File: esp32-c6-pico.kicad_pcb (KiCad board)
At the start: 4 copper layers, 20 x 29 mm, 65 parts, among them J1 USB4105-GF-A, J2 J2 GPIO / 2.00mm, J3 J3 GPIO / 2.00mm, SW1 RESET, SW2 BOOT, U1 ESP32-C6, U2 AP2112K-3.3, U3 W25Q32JVZPIQ, U4 SN74LV1T125, Y1 40MHz / CL=8pF

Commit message: optimize crystal rounting
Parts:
- moved R18 1.21 mm to (114.2, 115.0)
- moved C15 0.65 mm to (112.7, 114.7), turned to 90 degrees
- moved C4 0.59 mm to (116.1, 115.0), turned to 0 degrees
- moved C14 0.53 mm to (113.2, 117.4), turned to 90 degrees
- moved Y1 0.37 mm to (115.3, 116.9)
- moved C5 0.35 mm to (115.4, 118.8)
- moved C17 0.25 mm to (114.7, 113.0)
- moved C2 0.10 mm to (112.5, 113.0)
- moved L3 0.06 mm to (113.6, 113.4)
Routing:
- net USB_D-: track 33.3 -> 24.7 mm
- net GND: track 32.7 -> 27.5 mm, vias 48 -> 38
- net XTAL_LOAD_P: track 4.92 -> 2.38 mm
- net USB_D+: track 22.4 -> 24.1 mm
- net +3V3: track 69.4 -> 67.9 mm
- net XTAL_P: track 1.18 -> 2.47 mm
- net RF_50: track 3.48 -> 2.61 mm
- net VBUS_USB: track 40.7 -> 39.9 mm
- net XTAL_N: track 5.75 -> 5.21 mm

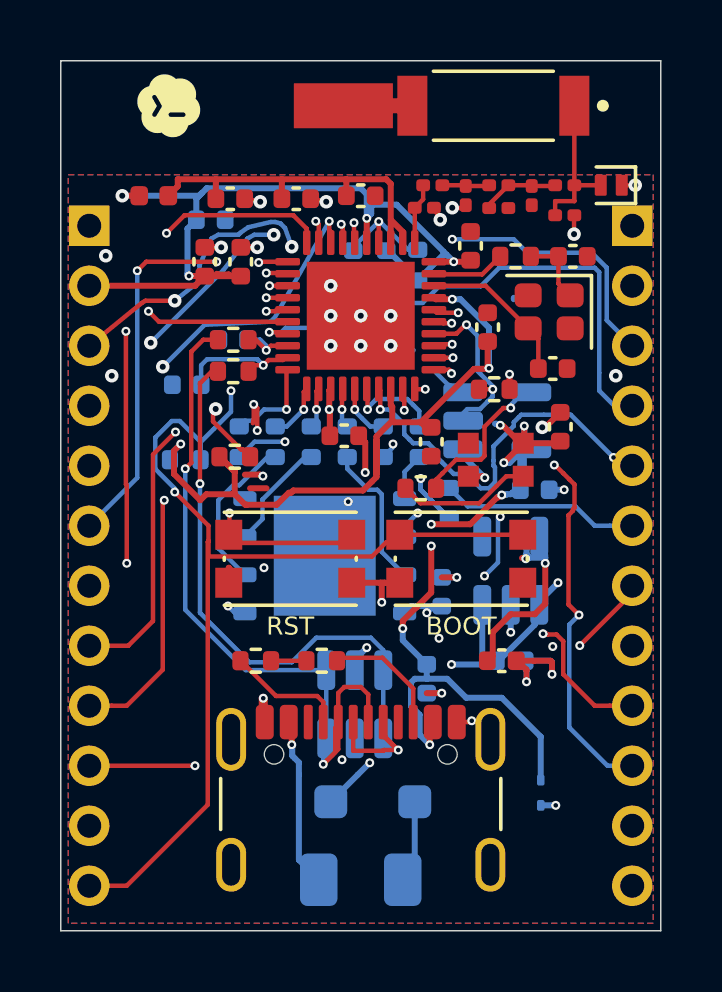
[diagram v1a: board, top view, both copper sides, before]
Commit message: Move headers inward by 0.3 mm and refresh layout outputs
Keep the 20 x 29 mm outline and move J2/J3 inward to a 17.50 mm
column spacing. Adjust local routing and labels, then refresh placement,
previews, geometry checks and fabrication notes. Preserve the subsequent
back-logo move and corrected drawing dimensions.

Validation: DRC, unconnected items and schematic parity all zero.
Independent QA passes 44/49 checks; the five failures predate this change.
Verified the input baseline and kept schematic, rules and RF/XTAL/USB
routing unchanged.
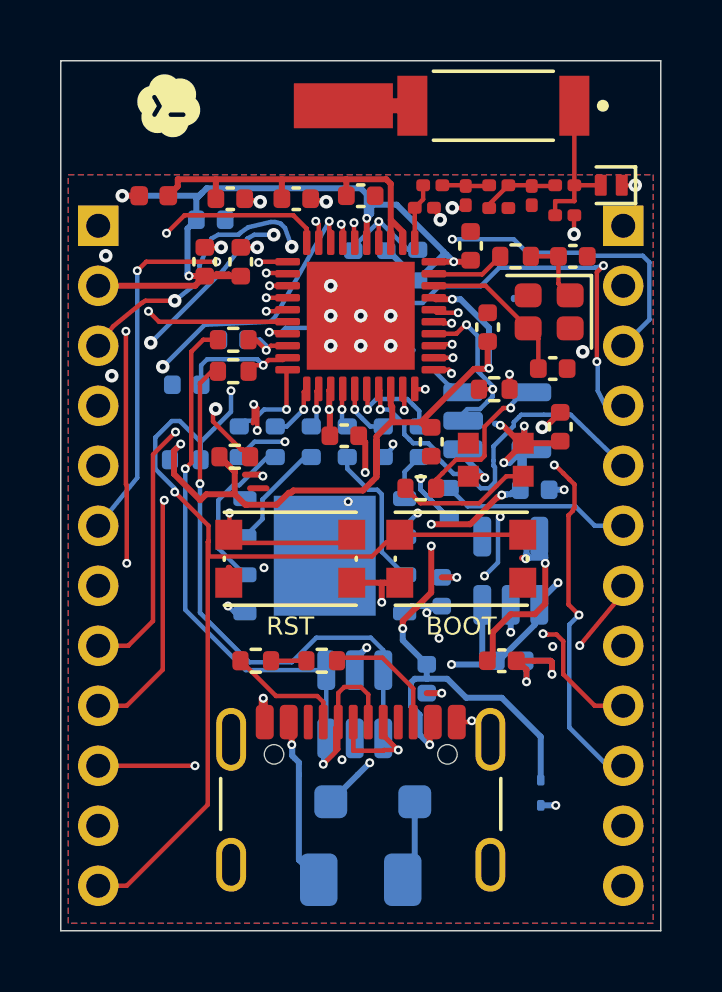
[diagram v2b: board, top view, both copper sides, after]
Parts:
- moved J2 0.30 mm to (100.2, 114.0)
- moved J3 0.30 mm to (117.8, 114.0)
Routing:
- net GPIO10: track 25.6 -> 27.2 mm
- net +5V: track 26.1 -> 27.6 mm
- net GPIO15: track 13.1 -> 12.7 mm, vias 2 -> 1
- net GPIO11: track 18.0 -> 18.3 mm, vias 1 -> 3
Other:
- board text added: "20 x 29 mm | 4 layers | 0.8 mm nominal | 0.20 mm drilled vias"
- board text removed: "20.5 x 32 mm | 4 layers | 0.8 mm nominal | 0.20 mm drilled vias"

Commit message: optimize USB vbus routing and other
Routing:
- net GND: track 27.5 -> 22.6 mm, vias 38 -> 36
- net VBUS_USB: track 39.9 -> 37.2 mm, vias 10 -> 8
- net GPIO20: track 19.6 -> 18.6 mm
- net GPIO15: track 12.7 -> 12.0 mm
- net U0TXD_MCU: track 7.38 -> 6.66 mm

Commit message: Restore SOIC-8 flash, shrink USB diode and remove input fuse
Use W25Q32JVSNIQ in a 150 mil SOIC-8 footprint and BAT760-7 in
SOD-323. Remove F1 and connect USB VBUS directly to the blocking
diode. Preserve the board outline and RF, crystal and USB data routing.

Synchronize schematics, BOM, placement, previews, fabrication notes and
independent checks. ERC, DRC, unconnected items and schematic parity
are all zero. QA passes 45 of 51 checks, retaining six pre-existing failures.
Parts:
- removed F1: 0.75A hold, Fuse:Fuse_1206_3216Metric
- D5: value SS14FL -> BAT760-7; footprint Diode_SMD:D_SOD-123F -> Diode_SMD:D_SOD-323
- U3: value W25Q32JVZPIQ -> W25Q32JVSNIQ; footprint Package_SON:WSON-8-1EP_6x5mm_P1.27mm_EP3.4x4mm -> Package_SO:SOIC-8_3.9x4.9mm_P1.27mm
- moved U3 0.22 mm to (107.6, 124.9)
- moved C6 0.10 mm to (111.8, 126.2)
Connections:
- D5 pad 2: VBUS_FUSED -> VBUS_USB
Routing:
- net VBUS_FUSED: track 2.77 -> 0.00 mm
- net SPI_CLK: track 4.18 -> 6.18 mm, vias 2 -> 0
- net U0TXD_MCU: track 6.66 -> 4.93 mm
- net VBUS_USB: track 37.2 -> 38.7 mm
- net SPI_CS: track 8.66 -> 7.22 mm
- net SPI_HD: track 4.89 -> 5.74 mm, vias 0 -> 2
- net SPI_Q: track 5.35 -> 6.04 mm

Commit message: move L2 into B.Cu and optimize routing
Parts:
- L2: moved to B.Cu
- moved L2 9.46 mm to (111.5, 112.7), turned to 180 degrees
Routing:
- net GPIO9_BOOT: track 38.3 -> 34.9 mm
- net +3V3: track 67.7 -> 66.5 mm, vias 9 -> 8
- net V3A: track 12.6 -> 11.8 mm, vias 0 -> 1
- net GPIO10: track 27.2 -> 26.6 mm
- net GPIO2: track 12.7 -> 13.3 mm
- net GND: vias 36 -> 35

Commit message: Complete first PCB revision
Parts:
- removed C26: 100nF, Capacitor_SMD:C_0402_1005Metric
- removed C27, C28: DNP, Capacitor_SMD:C_0402_1005Metric
- removed R12, R13: 22R, Resistor_SMD:R_0402_1005Metric
- removed U4: SN74LV1T125, Package_TO_SOT_SMD:SOT-23-5
- added D6: 1N4148WS, Diode_SMD:D_SOD-323, B.Cu at (113.9, 119.4)
- D2: footprint Pico:WS2812B_2020_Compact -> LED_SMD:LED_WS2812B-2020_PLCC4_2.0x2.0mm
- R14: moved to F.Cu
- R15: value 330R -> 0R
- R19: renamed from R16; value 100k -> 10k
- R9: value 10k -> 3.3k
- moved R9 5.50 mm to (104.7, 116.2)
- moved R15 4.72 mm to (115.7, 122.4), turned to -90 degrees
- moved R8 4.29 mm to (106.4, 119.0), turned to 90 degrees
- moved R14 2.73 mm to (111.0, 120.7), turned to 0 degrees
- moved R19 2.44 mm to (115.7, 120.4), turned to -90 degrees
- moved J2 2.00 mm to (102.2, 114.0)
- moved C14 1.58 mm to (114.0, 118.7), turned to 0 degrees
- moved C9 1.35 mm to (104.7, 114.2), turned to 0 degrees
- moved J1 1.00 mm to (110.0, 134.2)
- moved C8 0.74 mm to (104.2, 113.1), turned to -90 degrees
- moved C13 0.63 mm to (111.0, 121.7), turned to 0 degrees
- moved C5 0.55 mm to (116.0, 118.7)
- moved SW1 0.50 mm to (107.2, 125.1)
- moved SW2 0.50 mm to (112.8, 125.1)
- moved C10 0.33 mm to (104.7, 115.2), turned to 0 degrees
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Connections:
- J2 pad 1: GND -> GPIO1
- J2 pad 10: GPIO7 -> GPIO11
- J2 pad 11: GPIO8 -> +3V3
- J2 pad 12: GPIO9_BOOT -> GND
- J2 pad 2: +3V3 -> GPIO2
- J2 pad 3: GPIO0 -> GPIO3
- J2 pad 4: GPIO1 -> GPIO4
- J2 pad 5: GPIO2 -> GPIO5
- J2 pad 6: GPIO3 -> GPIO6
- J2 pad 7: GPIO4 -> GPIO7
- J2 pad 8: GPIO5 -> GPIO9_BOOT
- J2 pad 9: GPIO6 -> GPIO10
- J3 pad 1: +5V -> GPIO0
- J3 pad 10: GPIO20 -> GPIO15
- J3 pad 11: GPIO22 -> +5V
- J3 pad 12: GPIO23 -> GND
- J3 pad 2: GND -> GPIO23
- J3 pad 3: GPIO10 -> GPIO22
- J3 pad 4: GPIO11 -> GPIO21
- J3 pad 5: GPIO15 -> GPIO20
- J3 pad 6: U0TXD -> GPIO19
- J3 pad 7: U0RXD -> GPIO18
- J3 pad 8: GPIO18 -> U0TXD
- J3 pad 9: GPIO19 -> U0RXD
- R19 pad 1: GPIO21_LED -> VBUS_USB
- R19 pad 2: GND -> LED_DATA_5V
- U1 pad 18: USB_MCU_D- -> USB_D-
- U1 pad 19: USB_MCU_D+ -> USB_D+
- U1 pad 34: GPIO21_LED -> GPIO21
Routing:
- net GPIO23: track 25.3 -> 7.18 mm
- net GPIO22: track 21.4 -> 6.73 mm
- net GPIO8: track 24.0 -> 11.4 mm, vias 2 -> 1
- net GPIO10: track 26.6 -> 15.0 mm, vias 2 -> 0
- net GPIO20: track 18.6 -> 8.15 mm, vias 3 -> 1
- net GPIO4: track 18.6 -> 8.97 mm, vias 3 -> 1
- net GPIO7: track 22.4 -> 13.1 mm, vias 4 -> 1
- net GPIO9_BOOT: track 34.9 -> 25.9 mm, vias 3 -> 4
- net +5V: track 27.6 -> 19.1 mm, vias 3 -> 2
- net GPIO21: track 0.00 -> 7.31 mm, vias 0 -> 1
- net GPIO3: track 16.1 -> 8.79 mm, vias 3 -> 1
- net GPIO6: track 18.4 -> 11.3 mm, vias 2 -> 1
- net GPIO5: track 16.7 -> 9.77 mm, vias 2 -> 1
- net GPIO19: track 16.1 -> 9.69 mm, vias 4 -> 1
- net GPIO21_LED: track 6.36 -> 0.00 mm, vias 2 -> 0
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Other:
- board size 20 x 29 mm -> 18 x 29 mm
- board text added: "18 x 29 mm | 4 layers | 0.8 mm nominal | 0.20 mm drilled vias"
- board text added: "RFANT5220110A0T: 18 x 29 mm board, antenna on right; 18 x 3.8 mm no-pour region; RF validation required."
- board text removed: "20 x 29 mm | 4 layers | 0.8 mm nominal | 0.20 mm drilled vias"
- board text removed: "RFANT5220110A0T: 20 x 29 mm board, antenna on right; 20 x 3.8 mm no-pour region; RF validation required."
